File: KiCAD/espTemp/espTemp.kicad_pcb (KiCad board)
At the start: 2 copper layers, 38.1 x 25.4 mm, 7 parts, among them U1 ESP-01, U2 LD1117S33TR_SOT223, U3 DHT22,CM2303

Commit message: DHT22, DHT type
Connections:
- R1 pad 2: GPIO1 -> GPIO2
- U1 pad 2: GPIO1 -> Net-(U1-Pad2)
- U1 pad 3: Net-(U1-Pad3) -> GPIO2
- U3 pad 2: GPIO1 -> GPIO2
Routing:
- net GPIO1: track 60.0 -> 0.00 mm
- net GPIO2: track 0.00 -> 28.0 mm
- net +3V3: track 78.1 -> 70.3 mm, vias 2 -> 0
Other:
- board size 38.1 x 25.4 mm -> 36.2 x 23.5 mm

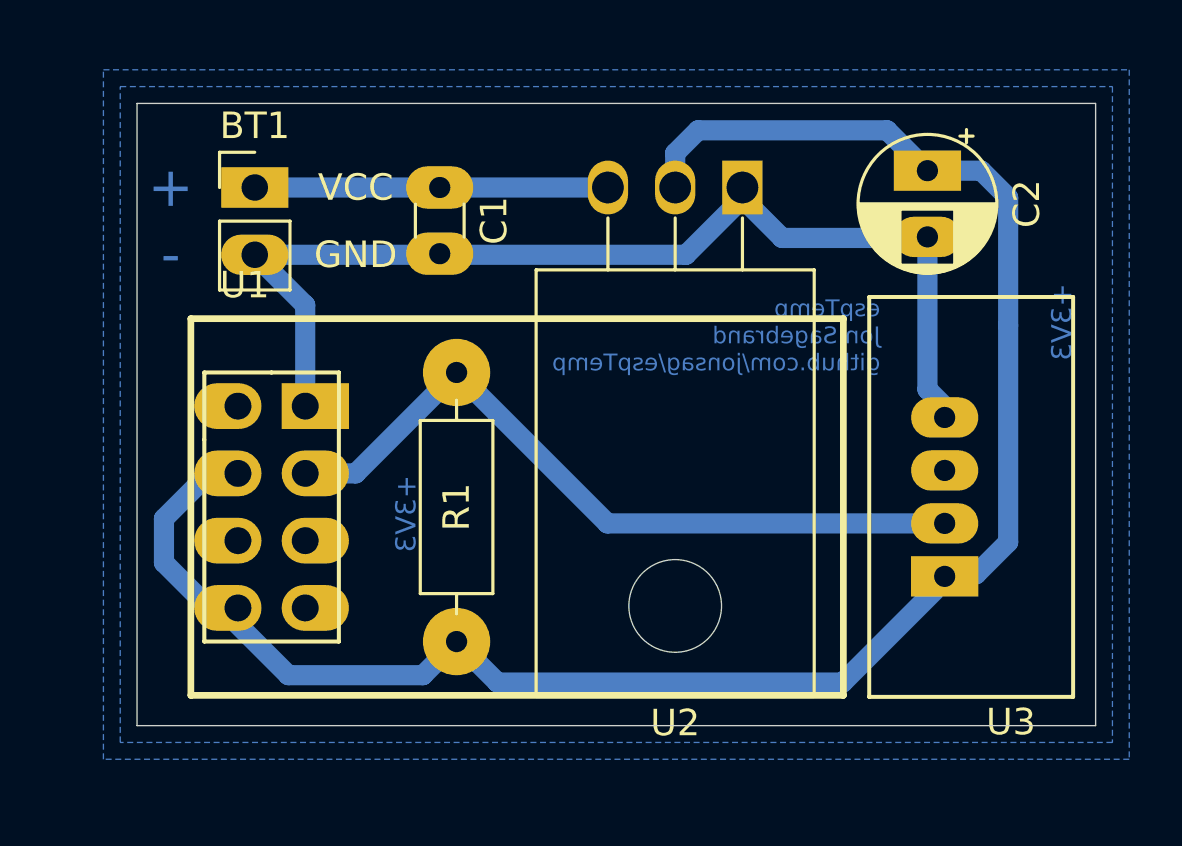
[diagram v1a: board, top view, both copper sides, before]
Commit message: 100mil DHT on PCB
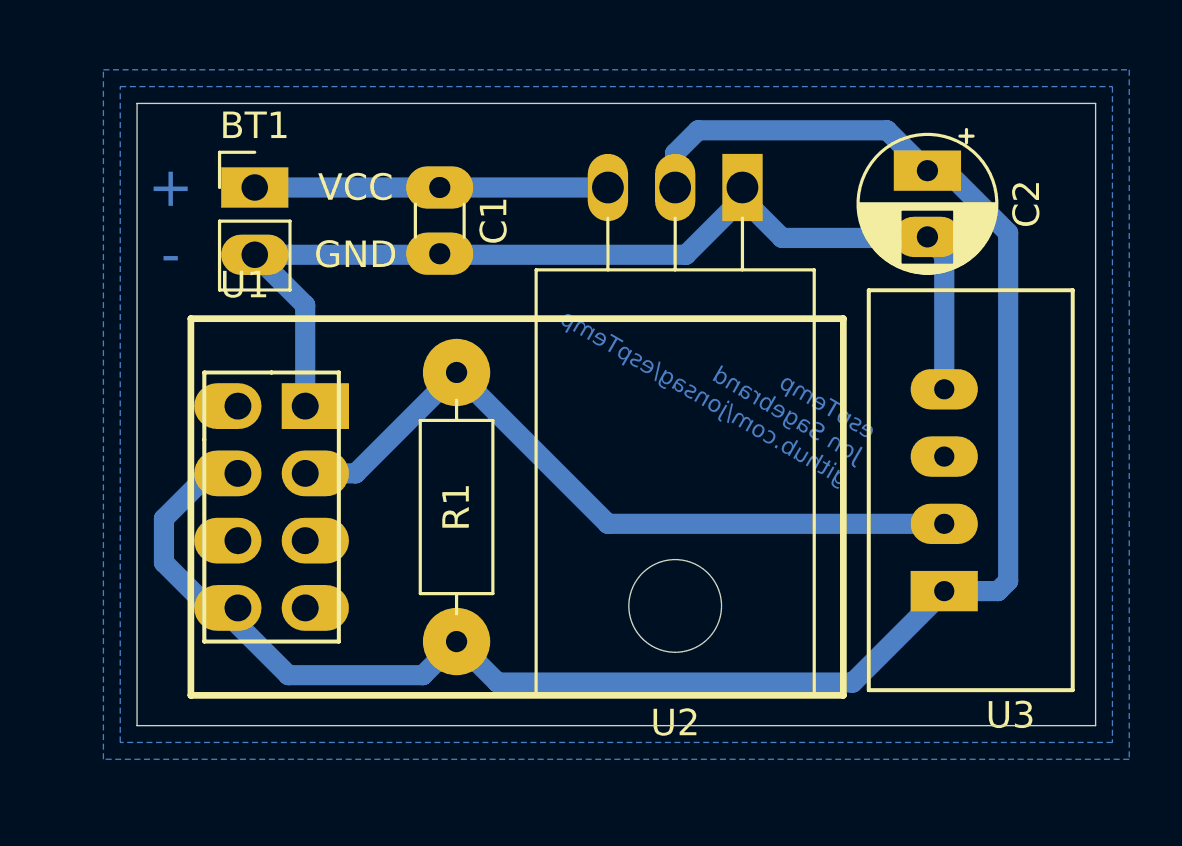
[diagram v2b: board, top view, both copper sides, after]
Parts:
- U3: footprint My_Misc:DHT22,RHT03,CM2303_large -> My_Parts:DHT22,RHT03,CM2303_100mil_large
- moved U3 3.70 mm to (164.5, 92.1)
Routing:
- net GND: track 40.0 -> 39.4 mm
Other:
- board text removed: "+3V3"

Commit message: KiCAD 6.x
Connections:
- U1 pad 2: Net-(U1-Pad2) -> unconnected-(U1-Pad2)
- U1 pad 5: Net-(U1-Pad5) -> unconnected-(U1-Pad5)
- U1 pad 6: Net-(U1-Pad6) -> unconnected-(U1-Pad6)
- U1 pad 7: Net-(U1-Pad7) -> unconnected-(U1-Pad7)
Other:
- net class Default removed

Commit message: 3d view
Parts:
- U1: footprint My_Arduino:ESP-01_large -> My_Arduino:ESP-01_w_pin_socket_large
- U2: footprint My_Misc:TO-220F-3_Horizontal_TabDown_large -> My_Misc:TO-220-3_Horizontal_TabDown_large
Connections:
- net GPIO2 renamed TempSignal
- U3 pad 3: Net-(U3-Pad3) -> unconnected-(U3-Pad3)
